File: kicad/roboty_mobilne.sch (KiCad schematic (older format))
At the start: 19 parts, among them J2 Conn_01x01, J3 Conn_01x04, SW3 SW_Push, SW4 SW_Push, U6 YAAJ_BluePill_Part_Like

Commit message: modified capacitors and cleaned up
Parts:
- J2: value Conn_01x01 -> ST-Link Pin
- J3: value Conn_01x04 -> UART Debug
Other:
- note removed: "ST-Link Pin"
- note removed: "UART Debug"
- moved on the sheet: J2, J3

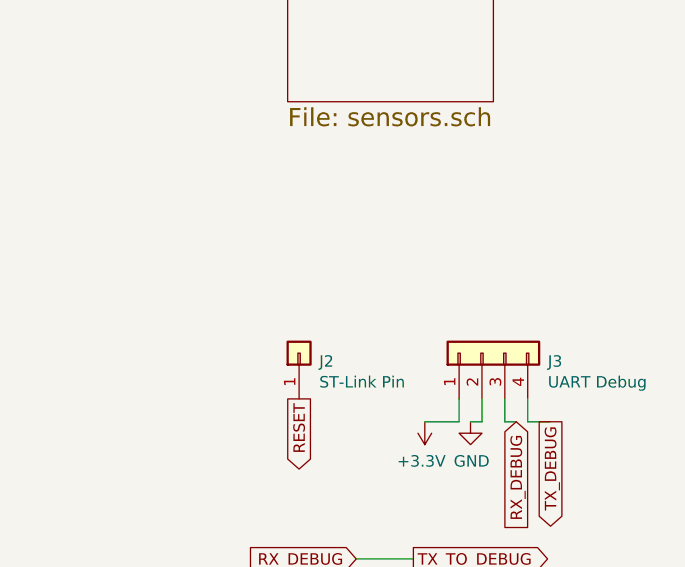
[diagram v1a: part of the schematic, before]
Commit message: modified capacitors near h bridge from 10u to 22u
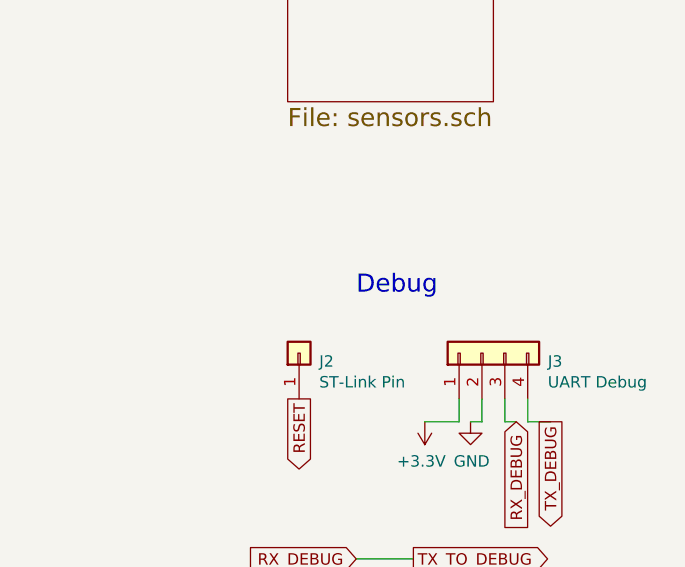
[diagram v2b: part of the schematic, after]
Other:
- note added: "Debug"
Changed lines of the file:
@@
 	1    0    0    -1
 $EndComp
+Text Notes 9850 4950 0    79   ~ 0
+Debug
 $EndSCHEMATC

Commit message: updated ladybug errors
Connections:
- no-connect marks 0 -> 13
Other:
- note added: "tutaj biedronka ma jakiś problem"
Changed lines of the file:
@@
 Text Notes 9850 4950 0    79   ~ 0
 Debug
+NoConn ~ 6450 4550
+NoConn ~ 6450 4450
+NoConn ~ 6450 4350
+NoConn ~ 6450 4250
+NoConn ~ 6450 4150
+NoConn ~ 6450 4050
+NoConn ~ 4850 4350
+NoConn ~ 4850 2950
+NoConn ~ 4850 2850
+NoConn ~ 6450 3050
+NoConn ~ 6450 3150
+NoConn ~ 6450 3250
+NoConn ~ 6450 3350
+Text Notes 4000 6900 0    50   ~ 0
+tutaj biedronka ma jakiś problem
 $EndSCHEMATC

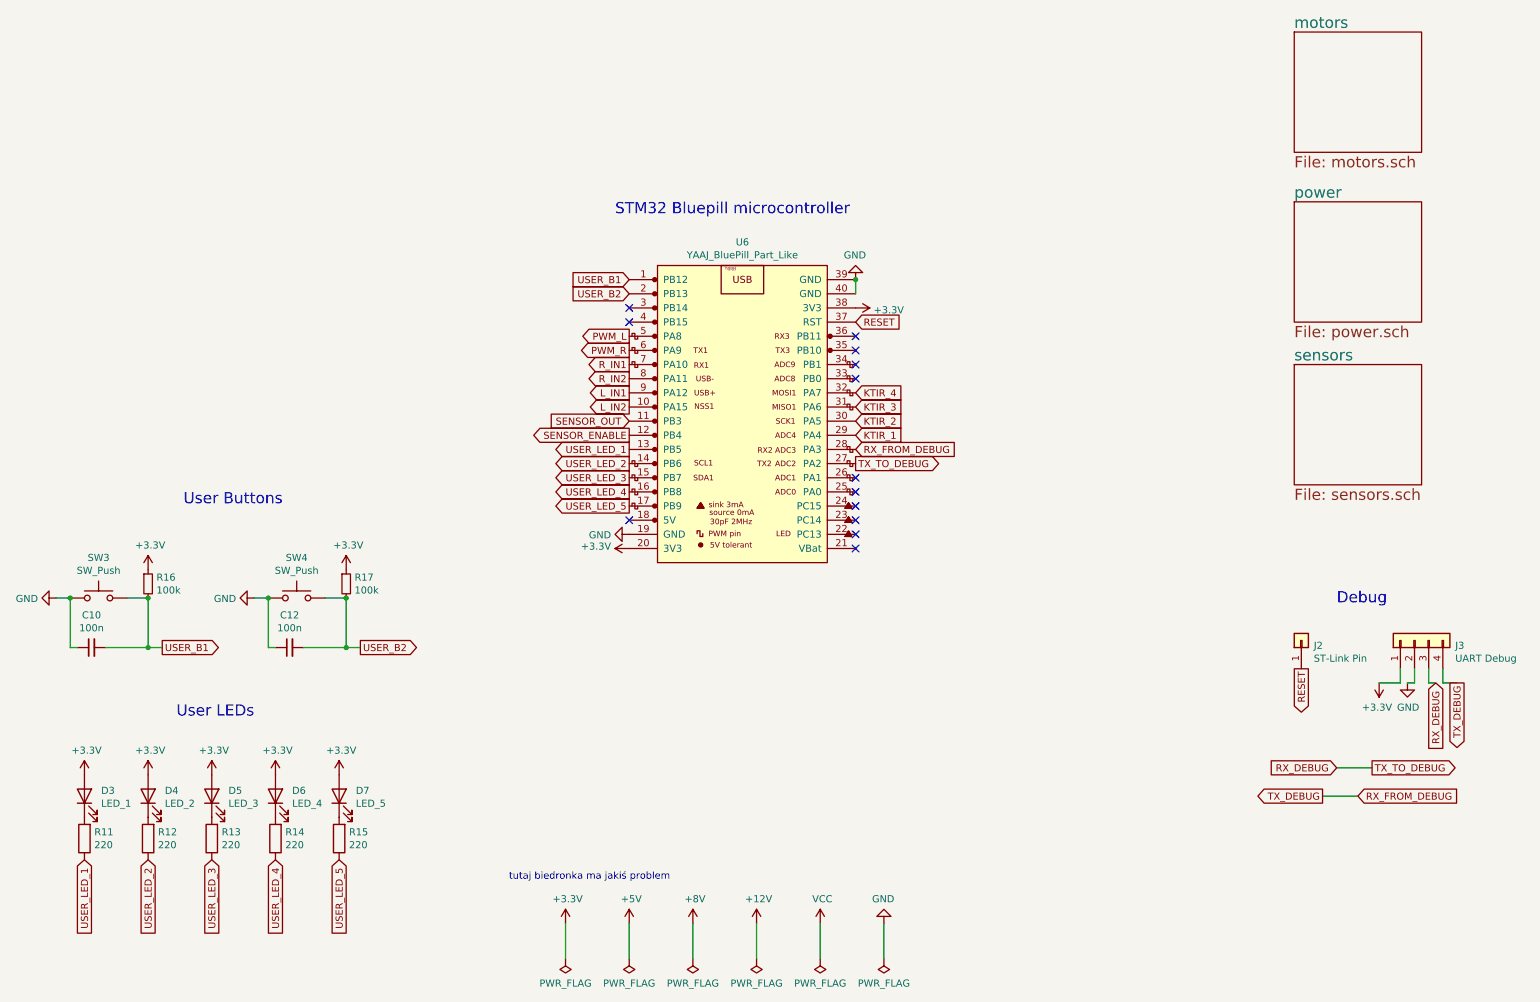
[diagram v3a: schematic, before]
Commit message: fixed diodes, h bridge and modified power supply
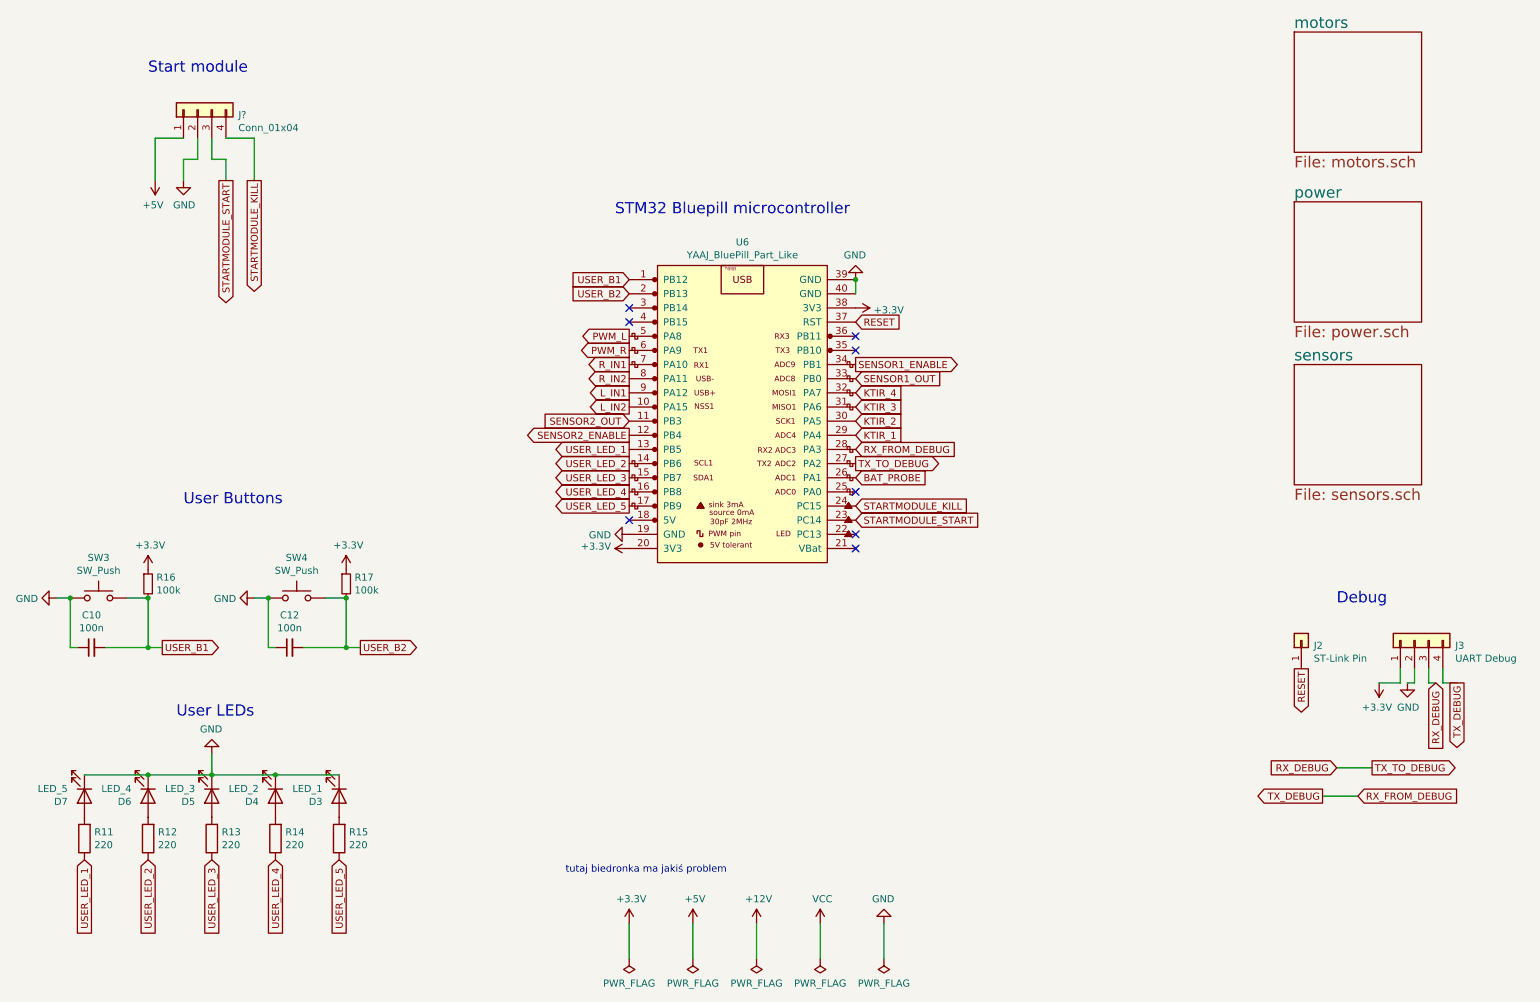
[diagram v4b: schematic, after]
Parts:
- added J?: Conn_01x04, symbol Connector_Generic:Conn_01x04
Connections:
- net +3V3: no longer D3.2 (A), D4.2 (A), D5.2 (A), D6.2 (A), D7.2 (A)
- net +5V: now also J?.1 (Pin_1)
- net GND: now also D3.1 (K), D4.1 (K), D5.1 (K), D6.1 (K), D7.1 (K), J?.2 (Pin_2)
- net STARTMODULE_START: now reaches U6.23 (PC14)
- net STARTMODULE_START: now also J?.3 (Pin_3)
- net STARTMODULE_KILL: now reaches U6.24 (PC15)
- net STARTMODULE_KILL: now also J?.4 (Pin_4)
- net BAT_PROBE: now reaches U6.26 (PA1)
- net SENSOR1_OUT: now reaches U6.33 (PB0)
- net SENSOR1_ENABLE: now reaches U6.34 (PB1)
- net at R11.2: now also D7.2 (A); no longer D3.1 (K)
- net at R12.2: now also D6.2 (A); no longer D4.1 (K)
- net at R13.2: now also D5.2 (A); no longer D5.1 (K)
- net at R14.2: now also D4.2 (A); no longer D6.1 (K)
- net at R15.2: now also D3.2 (A); no longer D7.1 (K)
- net SENSOR_ENABLE renamed SENSOR2_ENABLE
- net SENSOR_OUT renamed SENSOR2_OUT
- no-connect marks 13 -> 8
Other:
- note added: "Start module"
- moved on the sheet: D3, D4, D5, D6, D7
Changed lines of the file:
@@
 	-1   0    0    1
-$EndComp
-$Comp
-L Device:LED D7
-U 1 1 60A77E0D
-P 2800 6300
-F 0 "D7" V 2839 6182 50  0000 R CNN
-F 1 "LED_5" V 2748 6182 50  0000 R CNN
-F 2 "" H 2800 6300 50  0001 C CNN
-F 3 "~" H 2800 6300 50  0001 C CNN
-	1    2800 6300
-	0    -1   -1   0
-$EndComp
-$Comp
-L power:+3.3V #PWR015
-U 1 1 60A77E07
-P 2800 6150
-F 0 "#PWR015" H 2800 6000 50  0001 C CNN
-F 1 "+3.3V" H 2815 6323 50  0000 C CNN
-F 2 "" H 2800 6150 50  0001 C CNN
-F 3 "" H 2800 6150 50  0001 C CNN
-	1    2800 6150
-	1    0    0    -1
 $EndComp
 Text GLabel 2350 6750 3    50   Input ~ 0
@@
 	-1   0    0    1
 $EndComp
-$Comp
-L Device:LED D6
-U 1 1 60A68EA8
-P 2350 6300
-F 0 "D6" V 2389 6182 50  0000 R CNN
-F 1 "LED_4" V 2298 6182 50  0000 R CNN
-F 2 "" H 2350 6300 50  0001 C CNN
-F 3 "~" H 2350 6300 50  0001 C CNN
-	1    2350 6300
-	0    -1   -1   0
-$EndComp
-$Comp
-L power:+3.3V #PWR013
-U 1 1 60A68EA2
-P 2350 6150
-F 0 "#PWR013" H 2350 6000 50  0001 C CNN
-F 1 "+3.3V" H 2365 6323 50  0000 C CNN
-F 2 "" H 2350 6150 50  0001 C CNN
-F 3 "" H 2350 6150 50  0001 C CNN
-	1    2350 6150
-	1    0    0    -1
-$EndComp
 Text Notes 1650 5750 0    79   ~ 0
 User LEDs
@@
 	-1   0    0    1
 $EndComp
-$Comp
-L Device:LED D5
-U 1 1 60A5A534
-P 1900 6300
-F 0 "D5" V 1939 6182 50  0000 R CNN
-F 1 "LED_3" V 1848 6182 50  0000 R CNN
-F 2 "" H 1900 6300 50  0001 C CNN
-F 3 "~" H 1900 6300 50  0001 C CNN
-	1    1900 6300
-	0    -1   -1   0
-$EndComp
-$Comp
-L power:+3.3V #PWR012
-U 1 1 60A5A52E
-P 1900 6150
-F 0 "#PWR012" H 1900 6000 50  0001 C CNN
-F 1 "+3.3V" H 1915 6323 50  0000 C CNN
-F 2 "" H 1900 6150 50  0001 C CNN
-F 3 "" H 1900 6150 50  0001 C CNN
-	1    1900 6150
-	1    0    0    -1
-$EndComp
 Text GLabel 1450 6750 3    50   Input ~ 0
 USER_LED_2
@@
 	-1   0    0    1
 $EndComp
-$Comp
-L Device:LED D4
-U 1 1 60A5770C
-P 1450 6300
-F 0 "D4" V 1489 6182 50  0000 R CNN
-F 1 "LED_2" V 1398 6182 50  0000 R CNN
-F 2 "" H 1450 6300 50  0001 C CNN
-F 3 "~" H 1450 6300 50  0001 C CNN
-	1    1450 6300
-	0    -1   -1   0
-$EndComp
-$Comp
-L power:+3.3V #PWR011
-U 1 1 60A57706
-P 1450 6150
-F 0 "#PWR011" H 1450 6000 50  0001 C CNN
-F 1 "+3.3V" H 1465 6323 50  0000 C CNN
-F 2 "" H 1450 6150 50  0001 C CNN
-F 3 "" H 1450 6150 50  0001 C CNN
-	1    1450 6150
-	1    0    0    -1
-$EndComp
 Text GLabel 1000 6750 3    50   Input ~ 0
 USER_LED_1
@@
 	-1   0    0    1
 $EndComp
-$Comp
-L Device:LED D3
-U 1 1 60A4EEF4
-P 1000 6300
-F 0 "D3" V 1039 6182 50  0000 R CNN
-F 1 "LED_1" V 948 6182 50  0000 R CNN
-F 2 "" H 1000 6300 50  0001 C CNN
-F 3 "~" H 1000 6300 50  0001 C CNN
-	1    1000 6300
-	0    -1   -1   0
-$EndComp
-$Comp
-L power:+3.3V #PWR010
-U 1 1 60A4E6AA
-P 1000 6150
-F 0 "#PWR010" H 1000 6000 50  0001 C CNN
-F 1 "+3.3V" H 1015 6323 50  0000 C CNN
-F 2 "" H 1000 6150 50  0001 C CNN
-F 3 "" H 1000 6150 50  0001 C CNN
-	1    1000 6150
-	1    0    0    -1
-$EndComp
 Wire Wire Line
 	10300 5400 10300 5500
@@
 	5750 7200 5750 7450
 $Comp
-L power:PWR_FLAG #FLG0102
-U 1 1 60B800D4
+L power:PWR_FLAG #FLG0103
+U 1 1 60B80F42
 P 5300 7450
-F 0 "#FLG0102" H 5300 7525 50  0001 C CNN
+F 0 "#FLG0103" H 5300 7525 50  0001 C CNN
 F 1 "PWR_FLAG" H 5300 7623 50  0000 C CNN
 F 2 "" H 5300 7450 50  0001 C CNN
@@
 	5300 7200 5300 7450
 $Comp
-L power:PWR_FLAG #FLG0103
-U 1 1 60B80F42
+L power:+3.3V #PWR0102
+U 1 1 60AEF2CB
+P 4850 7200
+F 0 "#PWR0102" H 4850 7050 50  0001 C CNN
+F 1 "+3.3V" H 4865 7373 50  0000 C CNN
+F 2 "" H 4850 7200 50  0001 C CNN
+F 3 "" H 4850 7200 50  0001 C CNN
+	1    4850 7200
+	1    0    0    -1
+$EndComp
+$Comp
+L power:PWR_FLAG #FLG0104
+U 1 1 60AEF2D1
 P 4850 7450
-F 0 "#FLG0103" H 4850 7525 50  0001 C CNN
+F 0 "#FLG0104" H 4850 7525 50  0001 C CNN
 F 1 "PWR_FLAG" H 4850 7623 50  0000 C CNN
 F 2 "" H 4850 7450 50  0001 C CNN
@@
 Wire Wire Line
 	4850 7200 4850 7450
-$Comp
-L power:+8V #PWR0101
-U 1 1 60B90A42
-P 5300 7200
-F 0 "#PWR0101" H 5300 7050 50  0001 C CNN
-F 1 "+8V" H 5315 7373 50  0000 C CNN
-F 2 "" H 5300 7200 50  0001 C CNN
-F 3 "" H 5300 7200 50  0001 C CNN
-	1    5300 7200
-	1    0    0    -1
-$EndComp
-$Comp
-L power:+3.3V #PWR0102
-U 1 1 60AEF2CB
-P 4400 7200
-F 0 "#PWR0102" H 4400 7050 50  0001 C CNN
-F 1 "+3.3V" H 4415 7373 50  0000 C CNN
-F 2 "" H 4400 7200 50  0001 C CNN
-F 3 "" H 4400 7200 50  0001 C CNN
-	1    4400 7200
-	1    0    0    -1
-$EndComp
-$Comp
-L power:PWR_FLAG #FLG0104
-U 1 1 60AEF2D1
-P 4400 7450
-F 0 "#FLG0104" H 4400 7525 50  0001 C CNN
-F 1 "PWR_FLAG" H 4400 7623 50  0000 C CNN
-F 2 "" H 4400 7450 50  0001 C CNN
-F 3 "~" H 4400 7450 50  0001 C CNN
-	1    4400 7450
-	-1   0    0    1
-$EndComp
-Wire Wire Line
-	4400 7200 4400 7450
 $Comp
 L power:+12V #PWR0103
@@
 $EndComp
 Text GLabel 4850 3650 0    50   Input ~ 0
-SENSOR_OUT
+SENSOR2_OUT
 Text GLabel 4850 3750 0    50   Output ~ 0
-SENSOR_ENABLE
+SENSOR2_ENABLE
 Text GLabel 4850 3850 0    50   Output ~ 0
 USER_LED_1
@@
 L power:+5V #PWR0104
 U 1 1 60B056CF
-P 4850 7200
-F 0 "#PWR0104" H 4850 7050 50  0001 C CNN
-F 1 "+5V" H 4865 7373 50  0000 C CNN
-F 2 "" H 4850 7200 50  0001 C CNN
-F 3 "" H 4850 7200 50  0001 C CNN
-	1    4850 7200
+P 5300 7200
+F 0 "#PWR0104" H 5300 7050 50  0001 C CNN
+F 1 "+5V" H 5315 7373 50  0000 C CNN
+F 2 "" H 5300 7200 50  0001 C CNN
+F 3 "" H 5300 7200 50  0001 C CNN
+	1    5300 7200
 	1    0    0    -1
 $EndComp
@@
 NoConn ~ 6450 4550
 NoConn ~ 6450 4450
-NoConn ~ 6450 4350
-NoConn ~ 6450 4250
 NoConn ~ 6450 4150
-NoConn ~ 6450 4050
 NoConn ~ 4850 4350
 NoConn ~ 4850 2950
@@
 NoConn ~ 6450 3050
 NoConn ~ 6450 3150
-NoConn ~ 6450 3250
-NoConn ~ 6450 3350
-Text Notes 4000 6900 0    50   ~ 0
+Text Notes 4400 6850 0    50   ~ 0
 tutaj biedronka ma jakiś problem
+$Comp
+L Device:LED D7
+U 1 1 60A77E0D
+P 1000 6300
+F 0 "D7" V 1039 6182 50  0000 R CNN
+F 1 "LED_5" V 948 6182 50  0000 R CNN
+F 2 "" H 1000 6300 50  0001 C CNN
+F 3 "~" H 1000 6300 50  0001 C CNN
+	1    1000 6300
+	0    1    1    0
+$EndComp
+$Comp
+L Device:LED D6
+U 1 1 60A68EA8
+P 1450 6300
+F 0 "D6" V 1489 6182 50  0000 R CNN
+F 1 "LED_4" V 1398 6182 50  0000 R CNN
+F 2 "" H 1450 6300 50  0001 C CNN
+F 3 "~" H 1450 6300 50  0001 C CNN
+	1    1450 6300
+	0    1    1    0
+$EndComp
+$Comp
+L Device:LED D5
+U 1 1 60A5A534
+P 1900 6300
+F 0 "D5" V 1939 6182 50  0000 R CNN
+F 1 "LED_3" V 1848 6182 50  0000 R CNN
+F 2 "" H 1900 6300 50  0001 C CNN
+F 3 "~" H 1900 6300 50  0001 C CNN
+	1    1900 6300
+	0    1    1    0
+$EndComp
+$Comp
+L Device:LED D4
+U 1 1 60A5770C
+P 2350 6300
+F 0 "D4" V 2389 6182 50  0000 R CNN
+F 1 "LED_2" V 2298 6182 50  0000 R CNN
+F 2 "" H 2350 6300 50  0001 C CNN
+F 3 "~" H 2350 6300 50  0001 C CNN
+	1    2350 6300
+	0    1    1    0
+$EndComp
+$Comp
+L Device:LED D3
+U 1 1 60A4EEF4
+P 2800 6300
+F 0 "D3" V 2839 6182 50  0000 R CNN
+F 1 "LED_1" V 2748 6182 50  0000 R CNN
+F 2 "" H 2800 6300 50  0001 C CNN
+F 3 "~" H 2800 6300 50  0001 C CNN
+	1    2800 6300
+	0    1    1    0
+$EndComp
+$Comp
+L power:GND #PWR?
+U 1 1 60BF95BC
+P 1900 6000
+F 0 "#PWR?" H 1900 5750 50  0001 C CNN
+F 1 "GND" H 1905 5827 50  0000 C CNN
+F 2 "" H 1900 6000 50  0001 C CNN
+F 3 "" H 1900 6000 50  0001 C CNN
+	1    1900 6000
+	-1   0    0    1
+$EndComp
+Wire Wire Line
+	1900 6000 1900 6150
+Wire Wire Line
+	1900 6150 2350 6150
+Connection ~ 1900 6150
+Wire Wire Line
+	2350 6150 2800 6150
+Connection ~ 2350 6150
+Wire Wire Line
+	1900 6150 1450 6150
+Wire Wire Line
+	1450 6150 1000 6150
+Connection ~ 1450 6150
+Text GLabel 6450 3250 2    50   Output ~ 0
+SENSOR1_ENABLE
+Text GLabel 6450 3350 2    50   Input ~ 0
+SENSOR1_OUT
+Text GLabel 6450 4350 2    50   Input ~ 0
+STARTMODULE_START
+Text GLabel 6450 4250 2    50   Input ~ 0
+STARTMODULE_KILL
+Text Notes 1450 1200 0    79   ~ 0
+Start module
+$Comp
+L Connector_Generic:Conn_01x04 J?
+U 1 1 60C0AD19
+P 1800 1450
+F 0 "J?" V 1764 1162 50  0000 R CNN
+F 1 "Conn_01x04" V 1673 1162 50  0000 R CNN
+F 2 "" H 1800 1450 50  0001 C CNN
+F 3 "~" H 1800 1450 50  0001 C CNN
+	1    1800 1450
+	0    -1   -1   0
+$EndComp
+$Comp
+L power:+5V #PWR?
+U 1 1 60C0B99A
+P 1500 1950
+F 0 "#PWR?" H 1500 1800 50  0001 C CNN
+F 1 "+5V" H 1515 2123 50  0000 C CNN
+F 2 "" H 1500 1950 50  0001 C CNN
+F 3 "" H 1500 1950 50  0001 C CNN
+	1    1500 1950
+	-1   0    0    1
+$EndComp
+$Comp
+L power:GND #PWR?
+U 1 1 60C0DD49
+P 1700 1950
+F 0 "#PWR?" H 1700 1700 50  0001 C CNN
+F 1 "GND" H 1705 1777 50  0000 C CNN
+F 2 "" H 1700 1950 50  0001 C CNN
+F 3 "" H 1700 1950 50  0001 C CNN
+	1    1700 1950
+	1    0    0    -1
+$EndComp
+Text GLabel 2000 1950 3    50   Output ~ 0
+STARTMODULE_START
+Text GLabel 2200 1950 3    50   Output ~ 0
+STARTMODULE_KILL
+Wire Wire Line
+	2000 1650 2200 1650
+Wire Wire Line
+	2200 1650 2200 1950
+Wire Wire Line
+	1700 1650 1500 1650
+Wire Wire Line
+	1500 1650 1500 1950
+Wire Wire Line
+	1700 1950 1700 1800
+Wire Wire Line
+	1700 1800 1800 1800
+Wire Wire Line
+	1800 1800 1800 1650
+Wire Wire Line
+	2000 1950 2000 1800
+Wire Wire Line
+	2000 1800 1900 1800
+Wire Wire Line
+	1900 1800 1900 1650
+Text GLabel 6450 4050 2    50   Input ~ 0
+BAT_PROBE
 $EndSCHEMATC
